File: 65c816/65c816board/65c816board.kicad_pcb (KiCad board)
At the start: 2 copper layers, 27.9 x 88.9 mm, 10 parts, among them J1 Conn_01x34_Male, U1 w65c816, U2 74HC573, U3 74HC32, U4 74HC04

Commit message: Working setup for the 65c816
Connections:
- U3 pad 10: Net-(U3-Pad10) -> /5V
- U3 pad 12: /D7 -> Net-(U1-Pad35)
- U3 pad 13: /A15 -> /D7
- U3 pad 8: Net-(U2-Pad6) -> Net-(U3-Pad8)
- U3 pad 9: /D6 -> /5V
- U4 pad 12: Net-(U3-Pad10) -> Net-(U2-Pad6)
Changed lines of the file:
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@@
   (net 49 "Net-(U2-Pad19)")
   (net 50 "Net-(U3-Pad1)")
-  (net 51 "Net-(U3-Pad10)")
-  (net 52 "Net-(U3-Pad11)")
-  (net 53 "Net-(U4-Pad2)")
-  (net 54 "Net-(U4-Pad8)")
+  (net 51 "Net-(U3-Pad11)")
+  (net 52 "Net-(U4-Pad2)")
+  (net 53 "Net-(U4-Pad8)")
+  (net 54 "Net-(U3-Pad8)")
   (net_class Default "Dies ist die voreingestellte Netzklasse."
     (clearance 0.2)
@@
     (add_net "Net-(U2-Pad6)")
     (add_net "Net-(U3-Pad1)")
-    (add_net "Net-(U3-Pad10)")
     (add_net "Net-(U3-Pad11)")
+    (add_net "Net-(U3-Pad8)")
     (add_net "Net-(U4-Pad2)")
     (add_net "Net-(U4-Pad8)")
@@
       (net 50 "Net-(U3-Pad1)"))
     (pad 8 thru_hole oval (at 7.62 15.24) (size 1.6 1.6) (drill 0.8) (layers *.Cu *.Mask)
-      (net 45 "Net-(U2-Pad6)"))
+      (net 54 "Net-(U3-Pad8)"))
     (pad 2 thru_hole oval (at 0 2.54) (size 1.6 1.6) (drill 0.8) (layers *.Cu *.Mask)
       (net 3 /CLK))
     (pad 9 thru_hole oval (at 7.62 12.7) (size 1.6 1.6) (drill 0.8) (layers *.Cu *.Mask)
-      (net 28 /D6))
+      (net 2 /5V))
     (pad 3 thru_hole oval (at 0 5.08) (size 1.6 1.6) (drill 0.8) (layers *.Cu *.Mask)
       (net 6 /RD))
     (pad 10 thru_hole oval (at 7.62 10.16) (size 1.6 1.6) (drill 0.8) (layers *.Cu *.Mask)
-      (net 51 "Net-(U3-Pad10)"))
+      (net 2 /5V))
     (pad 4 thru_hole oval (at 0 7.62) (size 1.6 1.6) (drill 0.8) (layers *.Cu *.Mask)
       (net 39 "Net-(U1-Pad34)"))
     (pad 11 thru_hole oval (at 7.62 7.62) (size 1.6 1.6) (drill 0.8) (layers *.Cu *.Mask)
-      (net 52 "Net-(U3-Pad11)"))
+      (net 51 "Net-(U3-Pad11)"))
     (pad 5 thru_hole oval (at 0 10.16) (size 1.6 1.6) (drill 0.8) (layers *.Cu *.Mask)
       (net 3 /CLK))
     (pad 12 thru_hole oval (at 7.62 5.08) (size 1.6 1.6) (drill 0.8) (layers *.Cu *.Mask)
-      (net 27 /D7))
+      (net 40 "Net-(U1-Pad35)"))
     (pad 6 thru_hole oval (at 0 12.7) (size 1.6 1.6) (drill 0.8) (layers *.Cu *.Mask)
       (net 5 /WR))
     (pad 13 thru_hole oval (at 7.62 2.54) (size 1.6 1.6) (drill 0.8) (layers *.Cu *.Mask)
-      (net 11 /A15))
+      (net 27 /D7))
     (pad 7 thru_hole oval (at 0 15.24) (size 1.6 1.6) (drill 0.8) (layers *.Cu *.Mask)
       (net 1 /GND))
@@
       (net 1 /GND))
     (pad 13 thru_hole oval (at 7.62 2.54) (size 1.6 1.6) (drill 0.8) (layers *.Cu *.Mask)
-      (net 52 "Net-(U3-Pad11)"))
+      (net 51 "Net-(U3-Pad11)"))
     (pad 6 thru_hole oval (at 0 12.7) (size 1.6 1.6) (drill 0.8) (layers *.Cu *.Mask)
       (net 41 "Net-(U1-Pad37)"))
     (pad 12 thru_hole oval (at 7.62 5.08) (size 1.6 1.6) (drill 0.8) (layers *.Cu *.Mask)
-      (net 51 "Net-(U3-Pad10)"))
+      (net 45 "Net-(U2-Pad6)"))
     (pad 5 thru_hole oval (at 0 10.16) (size 1.6 1.6) (drill 0.8) (layers *.Cu *.Mask)
       (net 44 "Net-(U2-Pad11)"))
@@
       (net 50 "Net-(U3-Pad1)"))
     (pad 3 thru_hole oval (at 0 5.08) (size 1.6 1.6) (drill 0.8) (layers *.Cu *.Mask)
-      (net 53 "Net-(U4-Pad2)"))
+      (net 52 "Net-(U4-Pad2)"))
     (pad 9 thru_hole oval (at 7.62 12.7) (size 1.6 1.6) (drill 0.8) (layers *.Cu *.Mask)
       (net 2 /5V))
     (pad 2 thru_hole oval (at 0 2.54) (size 1.6 1.6) (drill 0.8) (layers *.Cu *.Mask)
-      (net 53 "Net-(U4-Pad2)"))
+      (net 52 "Net-(U4-Pad2)"))
     (pad 8 thru_hole oval (at 7.62 15.24) (size 1.6 1.6) (drill 0.8) (layers *.Cu *.Mask)
-      (net 54 "Net-(U4-Pad8)"))
+      (net 53 "Net-(U4-Pad8)"))
     (pad 1 thru_hole rect (at 0 0) (size 1.6 1.6) (drill 0.8) (layers *.Cu *.Mask)
       (net 3 /CLK))

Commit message: Remove unnecessary pullup at Rdy pin
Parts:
- removed R1: 1k, Resistor_THT:R_Axial_DIN0207_L6.3mm_D2.5mm_P7.62mm_Horizontal

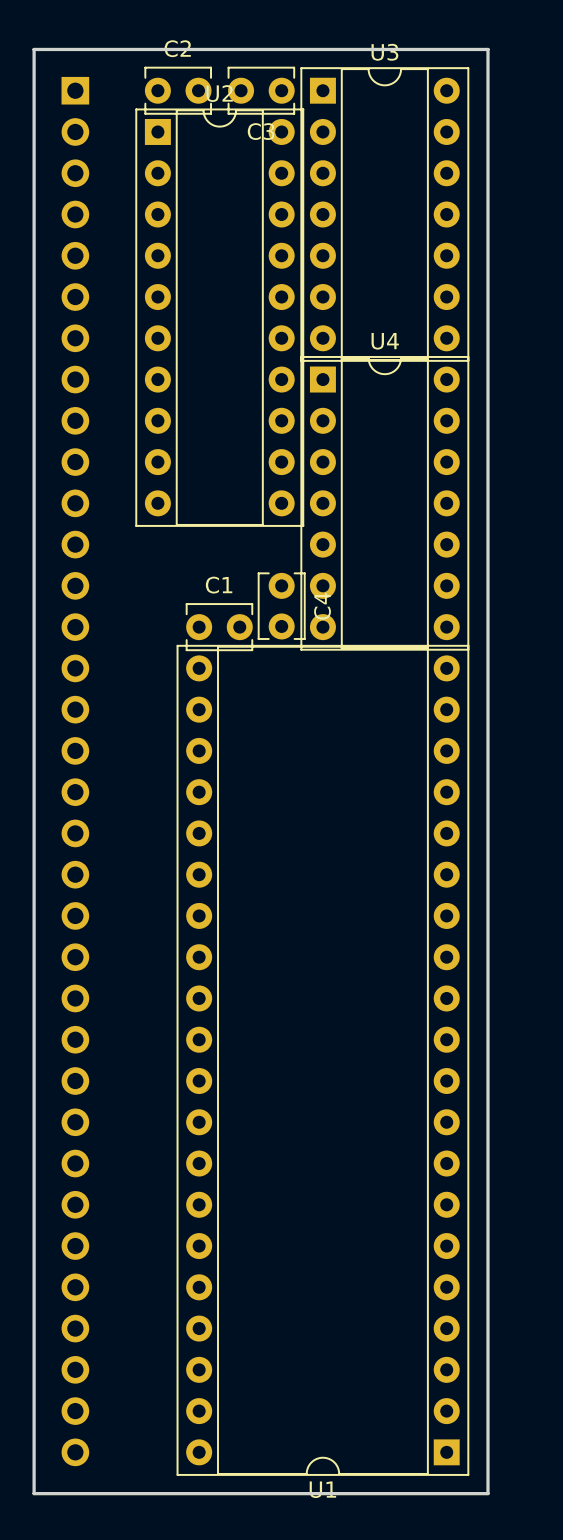
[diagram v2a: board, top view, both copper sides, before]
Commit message: Layout for 65C816 CPU board
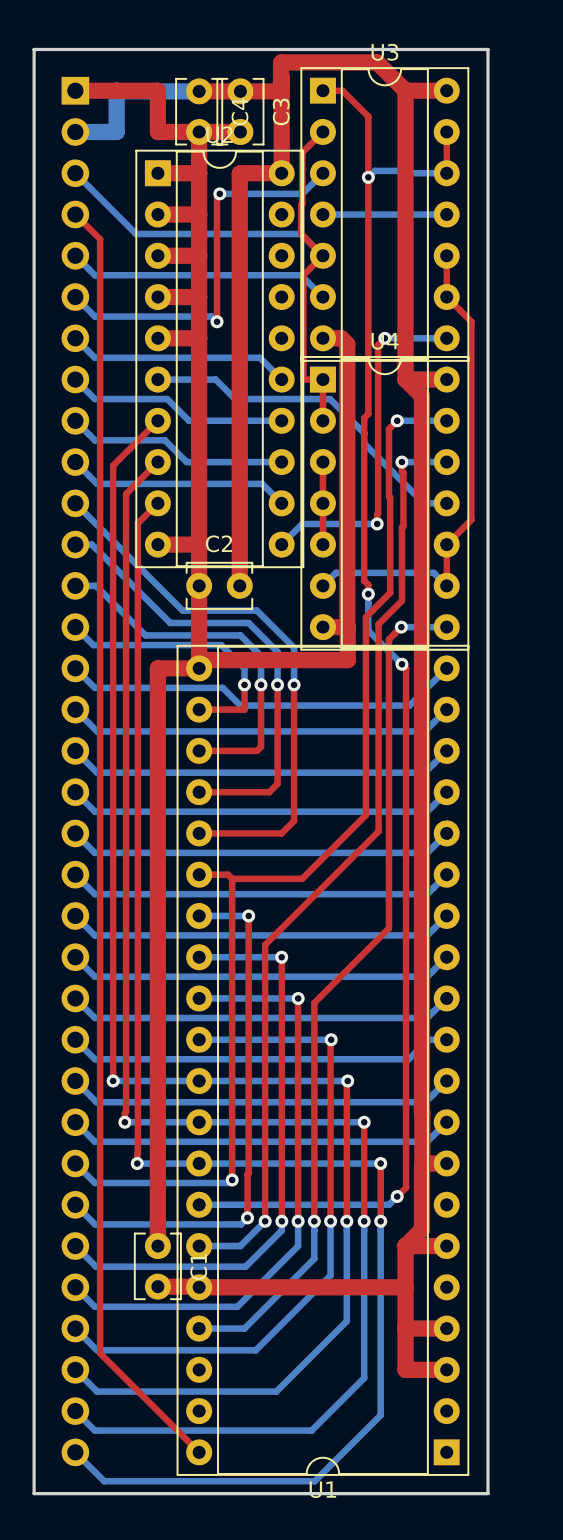
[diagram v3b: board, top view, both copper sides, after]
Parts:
- U2: value 74HC573 -> 74AC573
- U3: value 74HC32 -> 74AC00
- U4: value 74HC04 -> 74AC32
- moved C1 38.2 mm to (109.2, 132.1), turned to 270 degrees
- moved C4 30.9 mm to (111.8, 61.0)
- moved C2 30.6 mm to (111.8, 91.4)
- moved C3 2.54 mm to (114.3, 61.0), turned to 270 degrees
- moved U2 2.54 mm to (109.2, 66.0)
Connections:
- net /RAM renamed /ROM
- net /RD renamed /RD#
- net /RES renamed /RES#
- net /WR renamed /WR#
- U3 pad 1: Net-(U3-Pad1) -> Net-(U1-Pad34)
- U3 pad 10: /5V -> Net-(U3-Pad10)
- U3 pad 12: Net-(U1-Pad35) -> Net-(U1-Pad34)
- U3 pad 13: /D7 -> Net-(U1-Pad34)
- U3 pad 4: Net-(U1-Pad34) -> Net-(U3-Pad11)
- U3 pad 8: Net-(U3-Pad8) -> Net-(U2-Pad11)
- U3 pad 9: /5V -> Net-(U3-Pad10)
- U4 pad 10: Net-(U3-Pad1) -> Net-(U3-Pad10)
- U4 pad 11: Net-(U1-Pad34) -> Net-(U2-Pad6)
- U4 pad 12: Net-(U2-Pad6) -> Net-(U1-Pad35)
- U4 pad 13: Net-(U3-Pad11) -> /D7
- U4 pad 2: Net-(U4-Pad2) -> /CLK
- U4 pad 3: Net-(U4-Pad2) -> Net-(U4-Pad3)
- U4 pad 4: Net-(U2-Pad11) -> Net-(U4-Pad3)
- U4 pad 5: Net-(U2-Pad11) -> Net-(U4-Pad3)
- U4 pad 6: Net-(U1-Pad37) -> Net-(U3-Pad10)
- U4 pad 8: Net-(U4-Pad8) -> Net-(U1-Pad37)
- U4 pad 9: /5V -> Net-(U3-Pad10)
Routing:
- net /5V: track 0.00 -> 168.5 mm
- net /GND: track 0.00 -> 131.0 mm
- net /D0: track 0.00 -> 92.9 mm, vias 0 -> 3
- net /D1: track 0.00 -> 91.6 mm, vias 0 -> 3
- net Net-(U1-Pad34): track 0.00 -> 91.3 mm, vias 0 -> 4
- net /D2: track 0.00 -> 90.1 mm, vias 0 -> 3
- net /RES#: track 0.00 -> 79.4 mm
- net /D7: track 0.00 -> 68.9 mm, vias 0 -> 2
- net Net-(U1-Pad35): track 0.00 -> 57.8 mm, vias 0 -> 2
- net Net-(U1-Pad37): track 0.00 -> 52.8 mm, vias 0 -> 2
- net /D3: track 0.00 -> 40.8 mm, vias 0 -> 2
- net /CLK: track 0.00 -> 37.9 mm
- net /D4: track 0.00 -> 37.1 mm, vias 0 -> 2
- net /D5: track 0.00 -> 36.1 mm, vias 0 -> 2
- net /A15: track 0.00 -> 34.0 mm, vias 0 -> 1
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
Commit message: Better layout for 65c816 CPU board
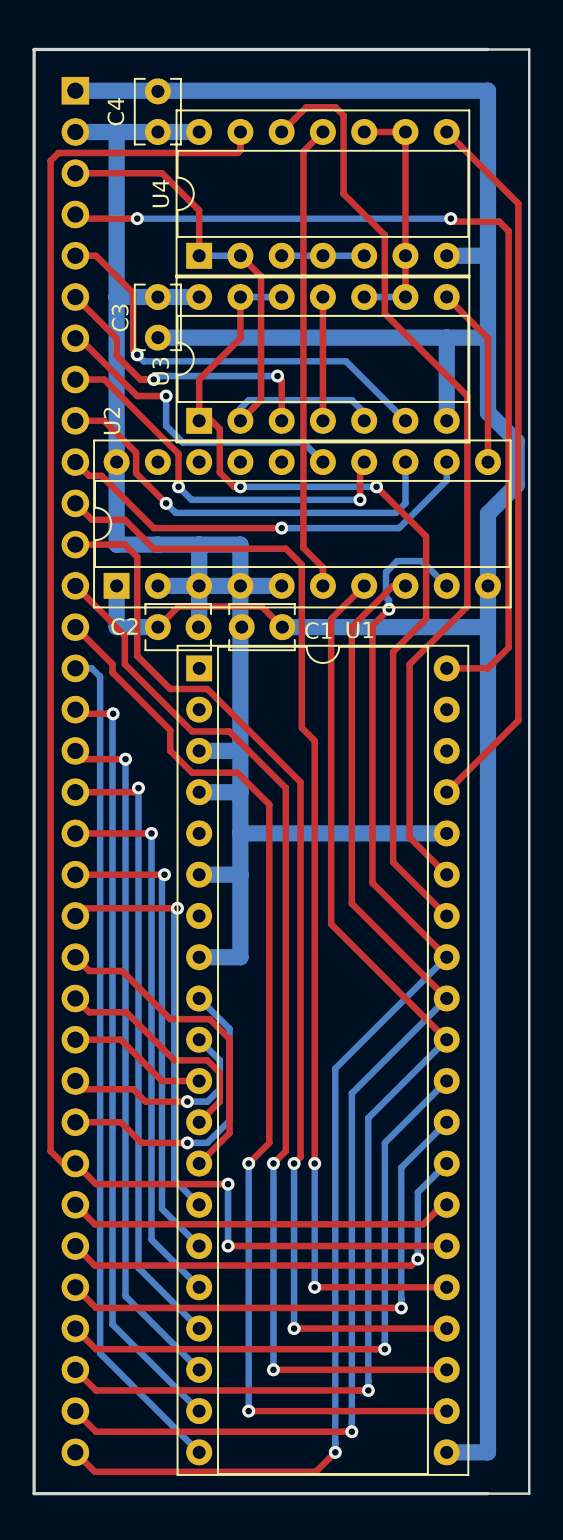
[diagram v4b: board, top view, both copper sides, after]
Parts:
- moved U1 50.6 mm to (111.8, 96.5), turned to 0 degrees
- moved C1 38.9 mm to (116.9, 94.0), turned to 180 degrees
- moved U2 25.5 mm to (106.7, 91.4), turned to 90 degrees
- moved U3 21.7 mm to (111.8, 81.3), turned to 90 degrees
- moved C3 13.6 mm to (109.2, 73.7)
- moved U4 10.8 mm to (111.8, 71.1), turned to 90 degrees
- moved C2 3.59 mm to (109.2, 94.0)
- moved C4 3.56 mm to (109.2, 63.5), turned to 90 degrees
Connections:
- U2 pad 2: /GND -> /5V
- U2 pad 3: /GND -> /5V
- U2 pad 4: /GND -> /5V
- U2 pad 5: /GND -> /5V
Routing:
- net /5V: track 168.5 -> 106.7 mm
- net /A12: track 16.8 -> 67.6 mm, vias 1 -> 2
- net /A13: track 22.7 -> 65.9 mm, vias 1 -> 2
- net /A14: track 28.3 -> 66.7 mm, vias 1 -> 2
- net /GND: track 131.0 -> 167.7 mm
- net Net-(U1-Pad34): track 91.3 -> 55.3 mm, vias 4 -> 2
- net /A15: track 34.0 -> 68.4 mm, vias 1 -> 2
- net /D7: track 68.9 -> 103.1 mm
- net /A11: track 24.8 -> 52.0 mm
- net /A10: track 24.0 -> 47.6 mm, vias 0 -> 1
- net /RES#: track 79.4 -> 57.1 mm, vias 0 -> 2
- net /A9: track 24.0 -> 42.8 mm, vias 0 -> 1
- net /D2: track 90.1 -> 73.9 mm, vias 3 -> 1
- net /D1: track 91.6 -> 76.3 mm, vias 3 -> 1
- net /A2: track 23.9 -> 8.67 mm
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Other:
- board size 27.9 x 88.9 mm -> 30.5 x 88.9 mm

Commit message: Production files for cpu board. More work on IO expander board
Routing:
- added copper zone on B.Cu, net /GND
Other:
- board text added: "Module for 65c816 https://github.com/ c0pperdragon/ByteMachine"
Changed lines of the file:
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@@
   (general
     (thickness 1.6)
-    (drawings 6)
+    (drawings 7)
     (tracks 383)
     (zones 0)
@@
   )
   (setup
-    (last_trace_width 0.4)
+    (last_trace_width 0.25)
     (user_trace_width 0.4)
     (user_trace_width 1)
@@
     (visible_elements 7FFFFFFF)
     (pcbplotparams
-      (layerselection 0x010fc_ffffffff)
+      (layerselection 0x010f0_ffffffff)
       (usegerberextensions false)
       (usegerberattributes false)
@@
       (outputformat 1)
       (mirror false)
-      (drillshape 1)
+      (drillshape 0)
       (scaleselection 1)
-      (outputdirectory ""))
+      (outputdirectory "65c816module/"))
   )
   (net 0 "")
@@
     )
   )
+  (gr_text "Module for 65c816\nhttps://github.com/\nc0pperdragon/ByteMachine" (at 117.856 124.968 90) (layer B.SilkS)
+    (effects (font (size 1.5 1.5) (thickness 0.3)) (justify mirror))
+  )
   (gr_line (start 132.08 147.32) (end 129.54 147.32) (layer Edge.Cuts) (width 0.15))
   (gr_line (start 132.08 58.42) (end 132.08 147.32) (layer Edge.Cuts) (width 0.15))
@@
   (segment (start 110.49 92.71) (end 115.61 92.71) (width 0.4) (layer F.Cu) (net 1))
   (segment (start 129.54 93.98) (end 116.88 93.98) (width 1) (layer B.Cu) (net 1))
-  (segment (start 111.72 134.58) (end 111.76 134.62) (width 1) (layer F.Cu) (net 15))
   (segment (start 106.68 63.5) (end 104.14 63.5) (width 1) (layer B.Cu) (net 2))
   (segment (start 106.68 63.5) (end 109.22 63.5) (width 1) (layer B.Cu) (net 2))
@@
   (segment (start 107.772 104.14) (end 104.14 104.14) (width 0.4) (layer F.Cu) (net 14))
   (segment (start 108.026 103.886) (end 107.772 104.14) (width 0.4) (layer F.Cu) (net 14))
+  (segment (start 111.72 134.58) (end 111.76 134.62) (width 1) (layer F.Cu) (net 15))
   (via (at 108.826 106.68) (size 0.8) (drill 0.4) (layers F.Cu B.Cu) (net 15))
   (segment (start 111.76 134.62) (end 108.826 131.686) (width 0.4) (layer B.Cu) (net 15))
@@
   (segment (start 116.84 71.12) (end 119.38 71.12) (width 0.4) (layer B.Cu) (net 52))
   (segment (start 121.92 71.12) (end 119.38 71.12) (width 0.4) (layer B.Cu) (net 52))
+  (zone (net 1) (net_name /GND) (layer B.Cu) (hatch edge 0.508)
+    (connect_pads yes (clearance 0.25))
+    (min_thickness 0.25)
+    (fill yes (arc_segments 16) (thermal_gap 0.508) (thermal_bridge_width 0.508))
+    (polygon
+      (pts
+        (xy 101.6 58.42) (xy 132.08 58.42) (xy 132.08 147.32) (xy 101.6 147.32)
+      )
+    )
+  )
 )
